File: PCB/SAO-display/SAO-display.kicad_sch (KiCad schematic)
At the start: 9 parts, among them CON1 SAO v1.69bis badge, J1 Conn_01x02, J2 Conn_01x02, J3 Conn_01x02, J4 Conn_01x02, J5 Conn_01x02, J6 Conn_01x02

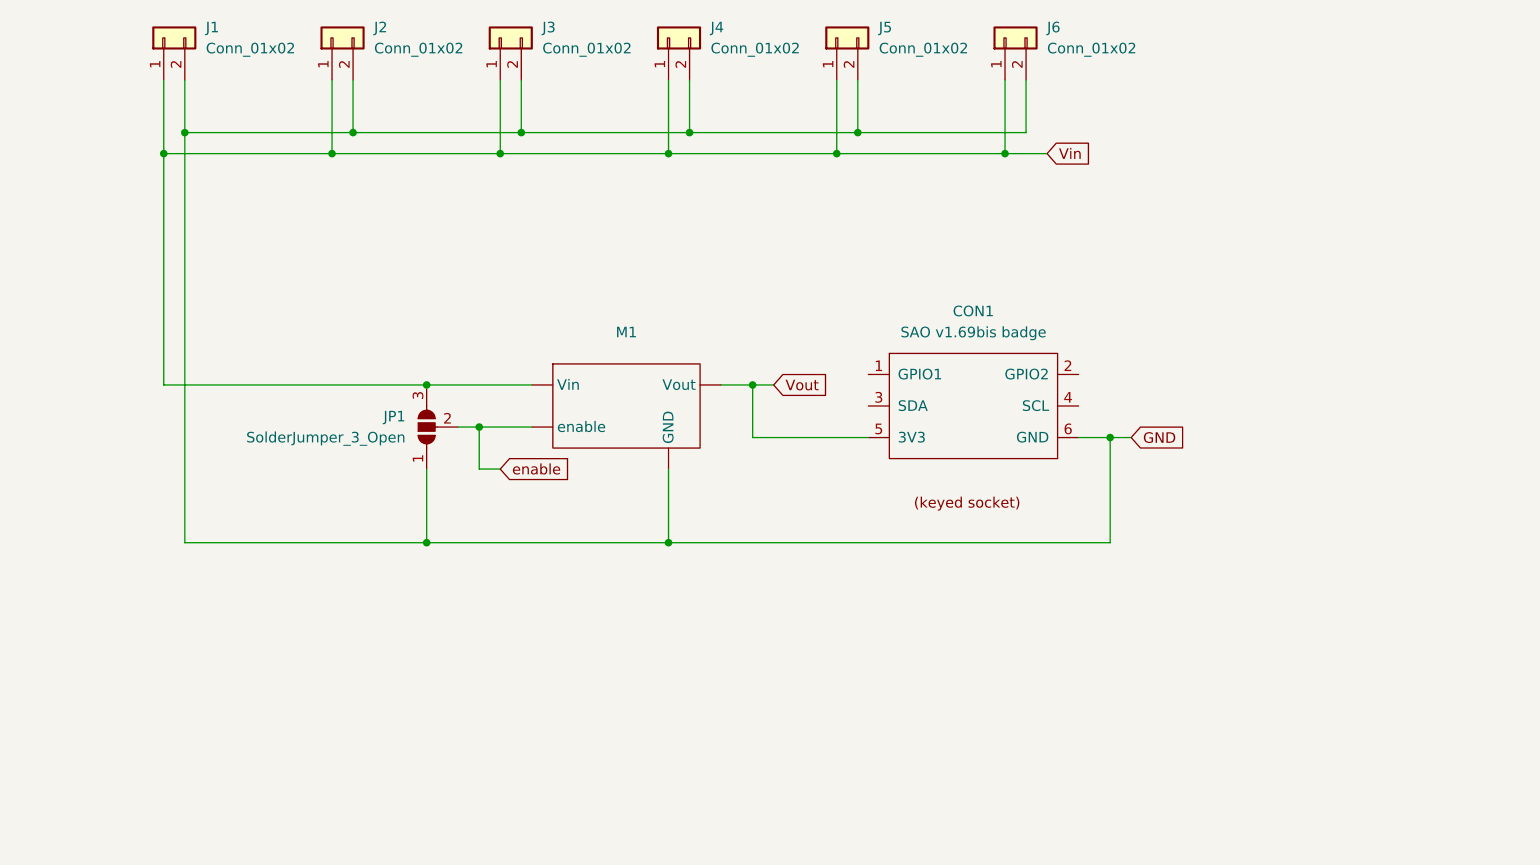
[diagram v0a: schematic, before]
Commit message: add decoupling capacitors
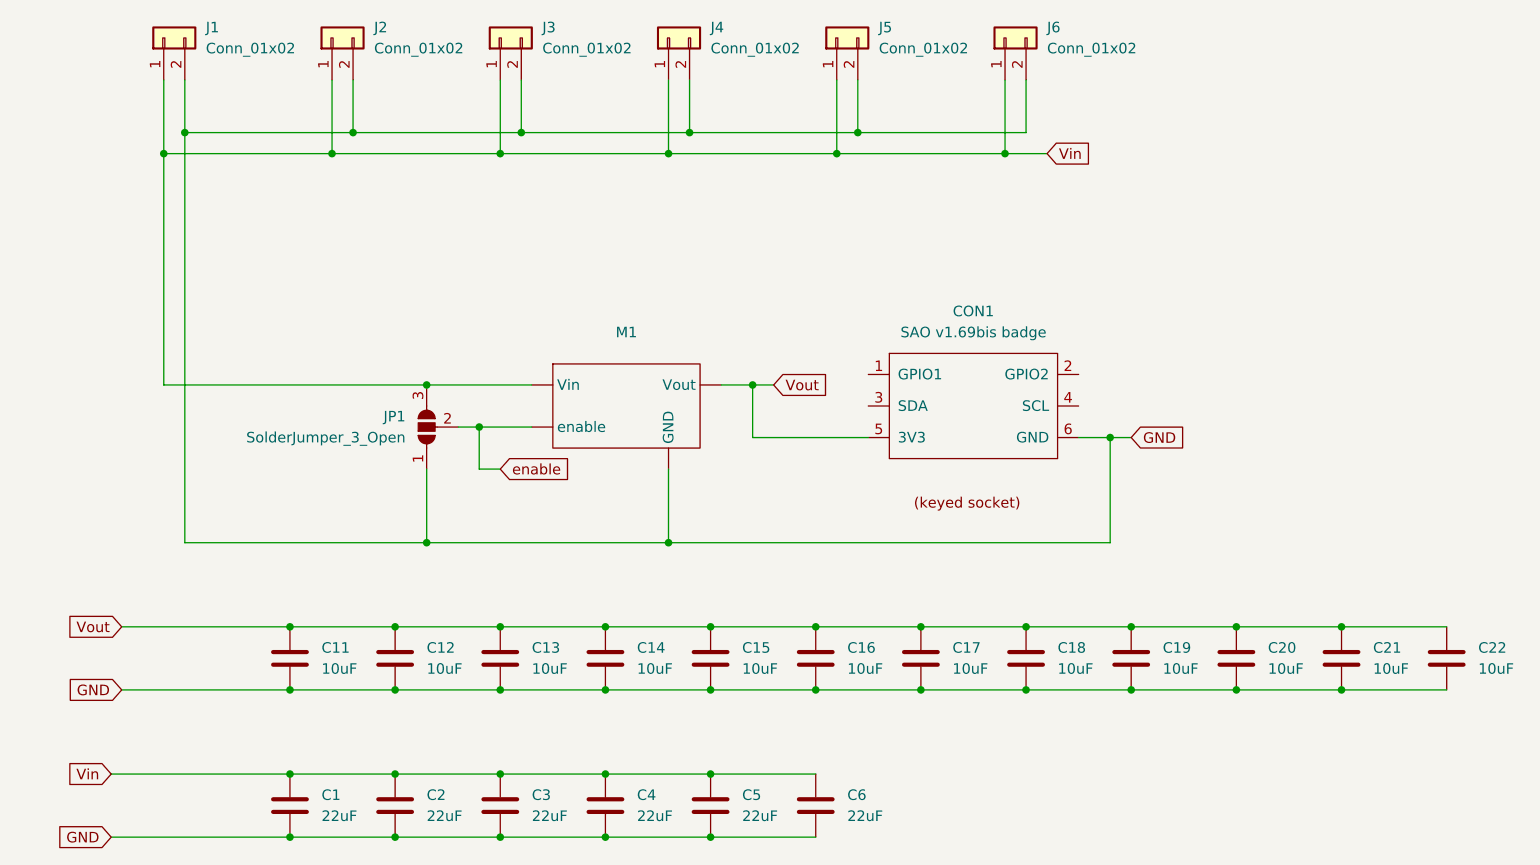
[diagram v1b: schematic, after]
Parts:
- added C1, C2, C3, C4, C5, C6: 22uF, Capacitor_SMD:C_0805_2012Metric_Pad1.18x1.45mm_HandSolder, symbol Device:C
- added C11, C12, C13, C14, C15, C16, C17, C18, C19, C20, C21, C22: 10uF, Capacitor_SMD:C_0402_1005Metric_Pad0.74x0.62mm_HandSolder, symbol Device:C
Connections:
- net GND: now also C1.2, C11.2, C12.2, C13.2, C14.2, C15.2, C16.2, C17.2, C18.2, C19.2, C2.2, C20.2, C21.2, C22.2, C3.2, C4.2, C5.2, C6.2
- net Vin: now also C1.1, C2.1, C3.1, C4.1, C5.1, C6.1
- net Vout: now also C11.1, C12.1, C13.1, C14.1, C15.1, C16.1, C17.1, C18.1, C19.1, C20.1, C21.1, C22.1

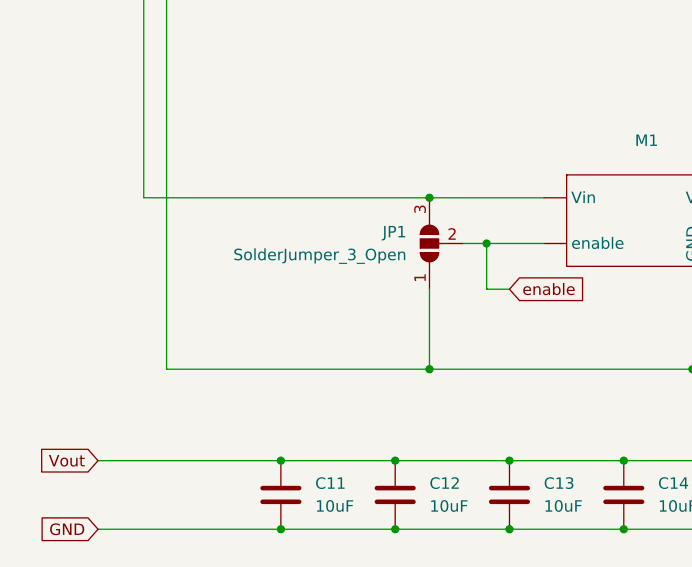
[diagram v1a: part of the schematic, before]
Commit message: add zener to protect input caps
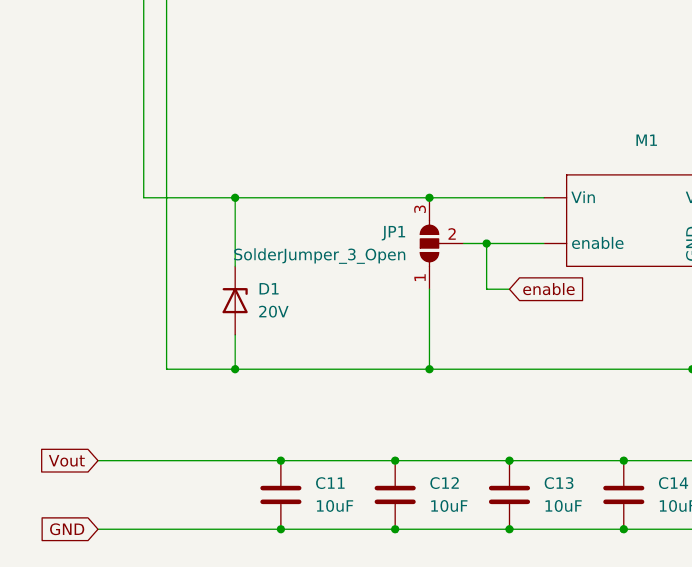
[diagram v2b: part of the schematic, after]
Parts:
- added D1: 20V, Diode_SMD:D_SOD-123, symbol Device:D_Zener
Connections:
- net GND: now also D1.2 (A)
- net Vin: now also D1.1 (K)
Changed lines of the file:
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@@
+	)
+	(junction
+		(at 41.91 67.31)
+		(diameter 0)
+		(color 0 0 0 0)
 	)
 	(junction
@@
 	)
 	(junction
+		(at 41.91 86.36)
+		(diameter 0)
+		(color 0 0 0 0)
+	)
+	(junction
 		(at 34.29 36.83)
 		(diameter 0)
@@
 	(wire
 		(pts
+			(xy 41.91 67.31) (xy 41.91 74.93)
+		)
+		(stroke
+			(width 0)
+			(type default)
+		)
+	)
+	(wire
+		(pts
 			(xy 97.79 96.52) (xy 85.09 96.52)
 		)
@@
 	(wire
 		(pts
-			(xy 34.29 86.36) (xy 63.5 86.36)
+			(xy 34.29 86.36) (xy 41.91 86.36)
+		)
+		(stroke
+			(width 0)
+			(type default)
+		)
+	)
+	(wire
+		(pts
+			(xy 41.91 67.31) (xy 63.5 67.31)
 		)
 		(stroke
@@
 	(wire
 		(pts
+			(xy 41.91 82.55) (xy 41.91 86.36)
+		)
+		(stroke
+			(width 0)
+			(type default)
+		)
+	)
+	(wire
+		(pts
 			(xy 97.79 121.92) (xy 85.09 121.92)
 		)
@@
 	(wire
 		(pts
+			(xy 41.91 86.36) (xy 63.5 86.36)
+		)
+		(stroke
+			(width 0)
+			(type default)
+		)
+	)
+	(wire
+		(pts
 			(xy 95.25 30.48) (xy 95.25 36.83)
 		)
@@
 	(wire
 		(pts
-			(xy 31.75 67.31) (xy 63.5 67.31)
+			(xy 31.75 67.31) (xy 41.91 67.31)
 		)
 		(stroke
@@
 					(unit 1)
 				)
+			)
+		)
+	)
+	(symbol
+		(lib_id "Device:D_Zener")
+		(at 41.91 78.74 270)
+		(unit 1)
+		(exclude_from_sim no)
+		(in_bom yes)
+		(on_board yes)
+		(dnp no)
+		(fields_autoplaced yes)
+		(property "Reference" "D1"
+			(at 44.45 77.4699 90)
+			(effects
+				(font
+					(size 1.27 1.27)
+				)
+				(justify left)
+			)
+		)
+		(property "Value" "20V"
+			(at 44.45 80.0099 90)
+			(effects
+				(font
+					(size 1.27 1.27)
+				)
+				(justify left)
+			)
+		)
+		(property "Footprint" "Diode_SMD:D_SOD-123"
+			(at 41.91 78.74 0)
+			(effects
+				(font
+					(size 1.27 1.27)
+				)
+				(hide yes)
+			)
+		)
+		(property "Datasheet" "~"
+			(at 41.91 78.74 0)
+			(effects
+				(font
+					(size 1.27 1.27)
+				)
+				(hide yes)
+			)
+		)
+		(property "Description" "Zener diode"
+			(at 41.91 78.74 0)
+			(effects
+				(font
+					(size 1.27 1.27)
+				)
+				(hide yes)
+			)
+		)
+		(pin "2"
+		)
+		(pin "1"
+		)
+		(instances
+			(project ""
+				(path "/d69956fb-1ece-4d71-a86e-9c0e03d8e4b0"
+					(reference "D1")
+					(unit 1)
+				)

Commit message: add LCSC part numbers
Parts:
- C1, C2, C3, C4, C5, C6: LCSC Part # (none) -> C602037
- C11, C12, C13, C14, C15, C16, C17, C18, C19, C20, C21, C22: LCSC Part # (none) -> C15525
- D1: LCSC Part # (none) -> C7544551

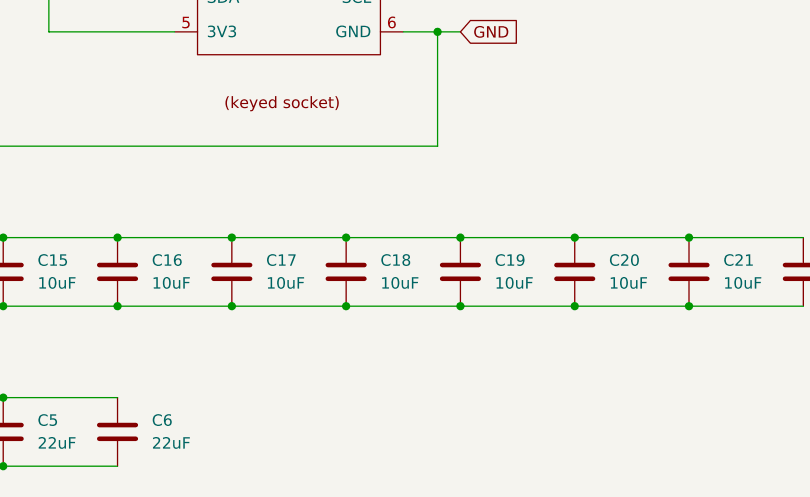
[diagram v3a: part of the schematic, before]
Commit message: add extra (larger) footprints for alternative capacitors
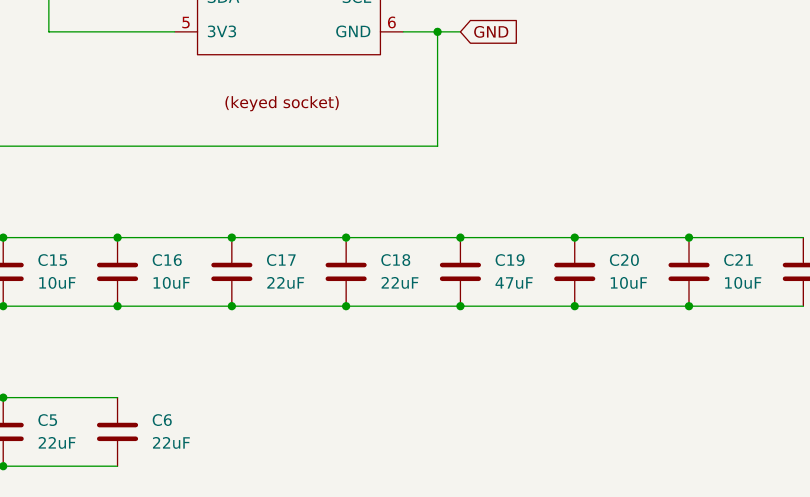
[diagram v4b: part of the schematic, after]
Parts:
- C17: value 10uF -> 22uF; footprint Capacitor_SMD:C_0402_1005Metric_Pad0.74x0.62mm_HandSolder -> Capacitor_SMD:C_0603_1608Metric; LCSC Part # C15525 -> C59461
- C18: value 10uF -> 22uF; footprint Capacitor_SMD:C_0402_1005Metric_Pad0.74x0.62mm_HandSolder -> Capacitor_SMD:C_0805_2012Metric; LCSC Part # C15525 -> C5674
- C19: value 10uF -> 47uF; footprint Capacitor_SMD:C_0402_1005Metric_Pad0.74x0.62mm_HandSolder -> Capacitor_SMD:C_1206_3216Metric; LCSC Part # C15525 -> C22399657

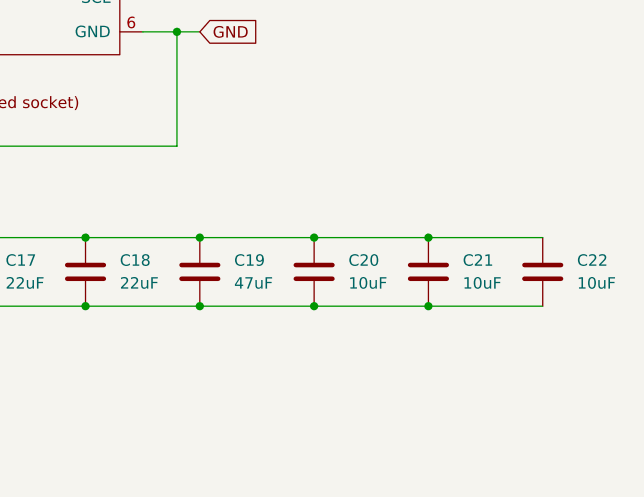
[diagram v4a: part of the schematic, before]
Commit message: add another alternative capacitor
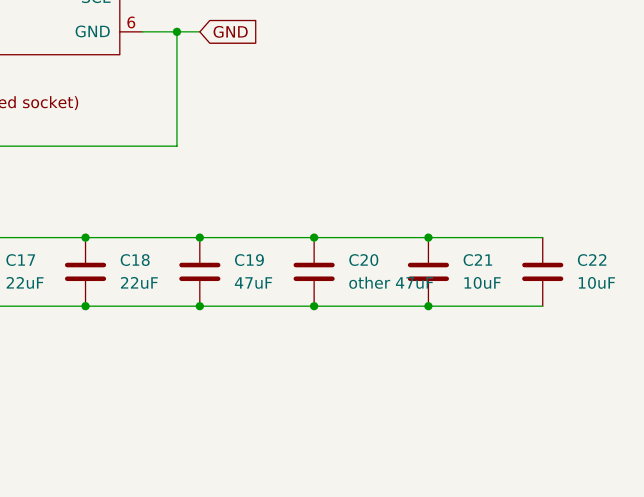
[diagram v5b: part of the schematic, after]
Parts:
- C20: value 10uF -> other 47uF; footprint Capacitor_SMD:C_0402_1005Metric_Pad0.74x0.62mm_HandSolder -> Capacitor_SMD:C_1206_3216Metric; LCSC Part # C15525 -> C68361
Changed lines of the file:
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@@
 			)
 		)
-		(property "Value" "10uF"
+		(property "Value" "other 47uF"
 			(at 165.1 101.5999 0)
 			(effects
@@
 			)
 		)
-		(property "Footprint" "Capacitor_SMD:C_0402_1005Metric_Pad0.74x0.62mm_HandSolder"
+		(property "Footprint" "Capacitor_SMD:C_1206_3216Metric"
 			(at 162.2552 104.14 0)
 			(effects
@@
 			)
 		)
-		(property "Datasheet" "https://www.lcsc.com/datasheet/lcsc_datasheet_2208231630_Samsung-Electro-Mechanics-CL05A106MQ5NUNC_C15525.pdf"
+		(property "Datasheet" "https://www.lcsc.com/datasheet/lcsc_datasheet_1810221121_Samsung-Electro-Mechanics-CL31A476MQHNNNE_C68361.pdf"
 			(at 161.29 100.33 0)
 			(effects
@@
 			)
 		)
-		(property "LCSC Part #" "C15525"
+		(property "LCSC Part #" "C68361"
 			(at 161.29 100.33 0)
 			(effects

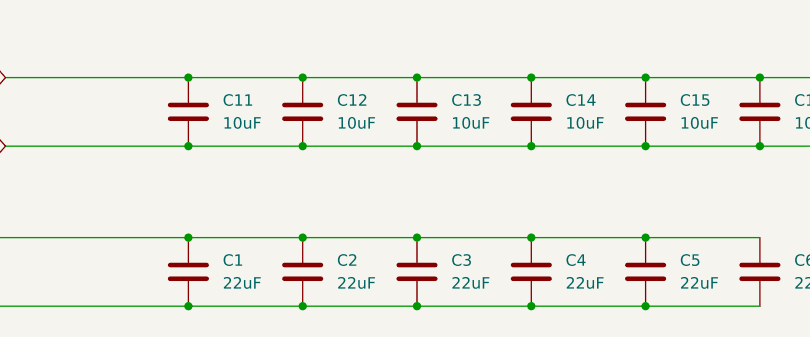
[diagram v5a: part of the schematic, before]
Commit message: add another alternative capacitor
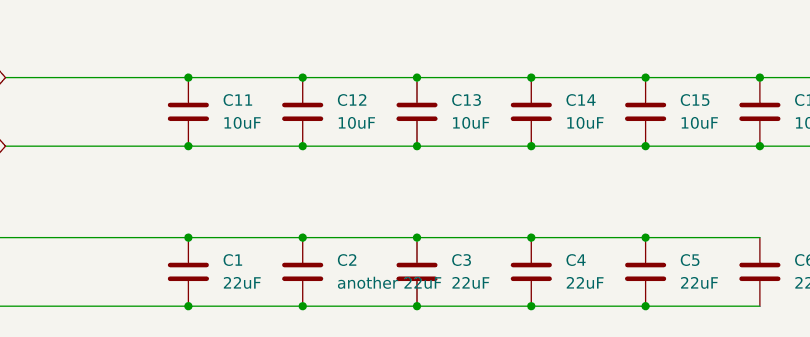
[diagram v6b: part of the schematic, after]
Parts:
- C2: value 22uF -> another 22uF; footprint Capacitor_SMD:C_0805_2012Metric_Pad1.18x1.45mm_HandSolder -> Capacitor_SMD:C_1206_3216Metric; LCSC Part # C602037 -> C7432786
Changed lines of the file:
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@@
 			)
 		)
-		(property "Value" "22uF"
+		(property "Value" "another 22uF"
 			(at 63.5 119.3799 0)
 			(effects
@@
 			)
 		)
-		(property "Footprint" "Capacitor_SMD:C_0805_2012Metric_Pad1.18x1.45mm_HandSolder"
+		(property "Footprint" "Capacitor_SMD:C_1206_3216Metric"
 			(at 60.6552 121.92 0)
 			(effects
@@
 			)
 		)
-		(property "Datasheet" "https://www.lcsc.com/datasheet/lcsc_datasheet_2006102223_Samsung-Electro-Mechanics-CL21A226MAYNNNE_C602037.pdf"
+		(property "Datasheet" "https://www.lcsc.com/datasheet/lcsc_datasheet_2410121645_Chinocera-HGC1206R5226M250NSPJ_C7432786.pdf"
 			(at 59.69 118.11 0)
 			(effects
@@
 			)
 		)
-		(property "LCSC Part #" "C602037"
+		(property "LCSC Part #" "C7432786"
 			(at 59.69 118.11 0)
 			(effects
